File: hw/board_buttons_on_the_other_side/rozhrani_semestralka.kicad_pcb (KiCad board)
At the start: 2 copper layers, 152 x 47 mm, 63 parts, among them P1 DISPLAY_CONN, P2 DISPLAY_VCC_CON, P3 USB_B, U1 MCP2210, U2 MIC5504-3.3, U3 Joystick, U4 LM239, U5 CD4532, U6 NPIC6C596, U7 NE555, U8 PB6149L, U9 PB6149L

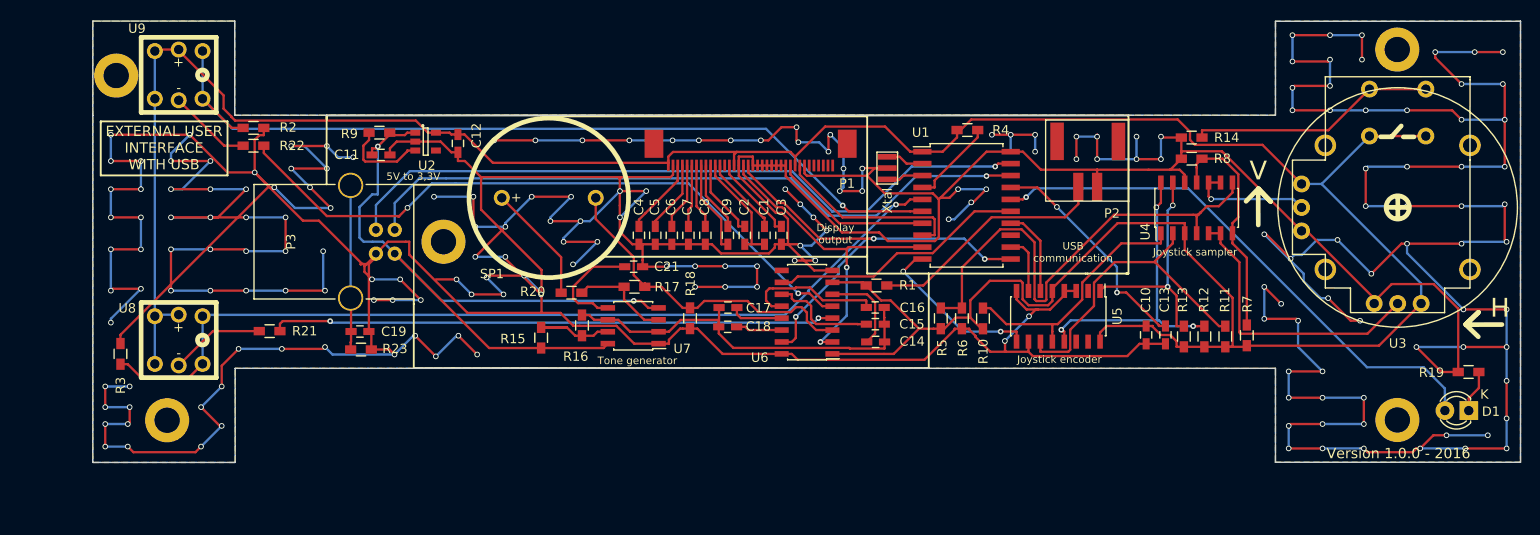
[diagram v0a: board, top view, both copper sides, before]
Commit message: first revision of caseing
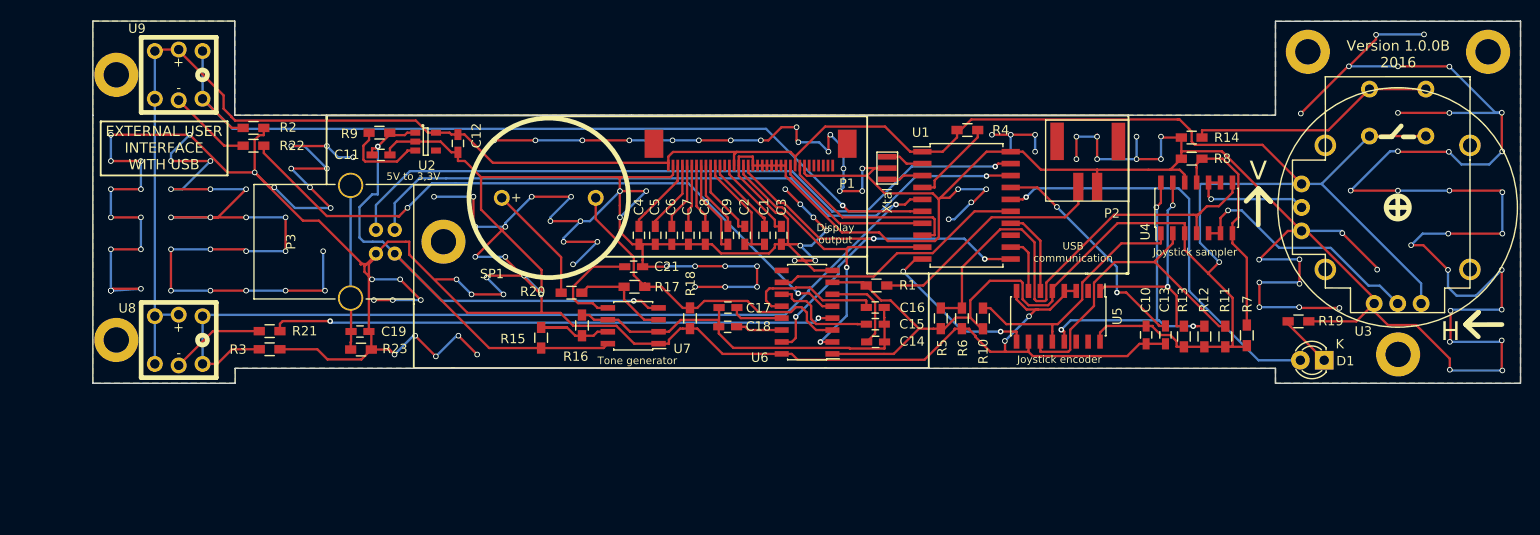
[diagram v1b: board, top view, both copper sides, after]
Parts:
- added REF**: MountingHole_2.7mm_M2.5_DIN965_Pad, Mounting_Holes:MountingHole_2.7mm_M2.5_DIN965_Pad, F.Cu at (213.7, 118.2)
- moved REF** 40.3 mm to (204.0, 86.0)
- moved R19 18.9 mm to (203.0, 114.7), turned to 180 degrees
- moved D1 16.3 mm to (205.8, 118.8)
- moved R3 15.9 mm to (93.5, 117.6), turned to 0 degrees
- moved REF** 10.1 mm to (77.2, 116.7)
- moved REF** 9.67 mm to (223.2, 86.0)
- moved REF** 0.08 mm to (77.2, 88.4)
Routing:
- net GND: track 1130.6 -> 966.4 mm, vias 195 -> 153
- net /SIGNAL_LED: track 57.9 -> 44.7 mm
- net Net-(U3-Pad9): track 30.9 -> 26.2 mm, vias 0 -> 1
- net /BUT1: track 96.8 -> 93.6 mm
- net Net-(D1-Pad1): track 4.56 -> 6.30 mm
- net +3V3: track 324.2 -> 325.5 mm, vias 0 -> 1
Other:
- board size 152 x 47 mm -> 152 x 38.6 mm
- board text added: "Version 1.0.0B 2016"
- board text removed: "Version 1.0.0 - 2016"

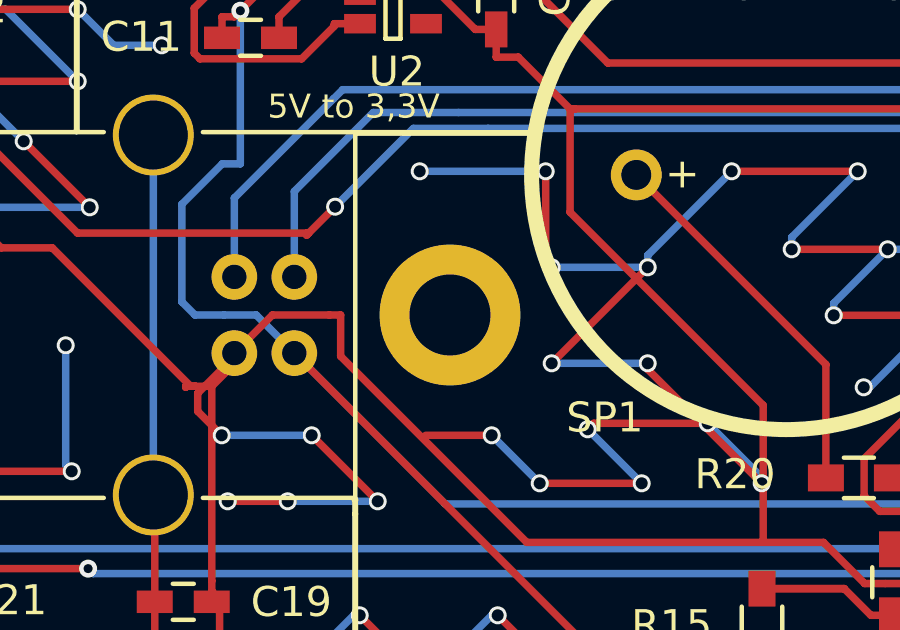
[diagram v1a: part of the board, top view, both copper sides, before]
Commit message: Just remove one mounting hole
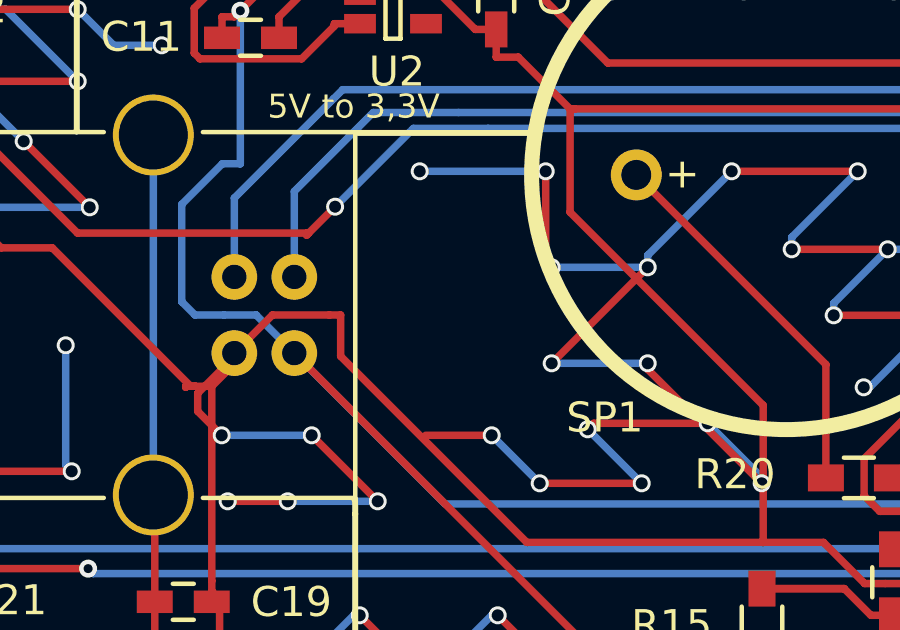
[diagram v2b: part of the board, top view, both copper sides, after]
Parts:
- removed the REF** at (112.0, 106.2)
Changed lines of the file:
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@@
     (tracks 1166)
     (zones 0)
-    (modules 64)
+    (modules 63)
     (nets 73)
   )
@@
   (module Mounting_Holes:MountingHole_2.7mm_M2.5_DIN965_Pad (layer F.Cu)
     (at 77.18 88.42)
-    (descr "Mounting Hole 2.7mm, M2.5, DIN965")
-    (tags "mounting hole 2.7mm m2.5 din965")
-    (fp_text reference REF** (at 0 -3.35) (layer Dwgs.User)
-      (effects (font (size 1 1) (thickness 0.15)))
-    )
-    (fp_text value MountingHole_2.7mm_M2.5_DIN965_Pad (at 0 3.35) (layer F.Fab)
-      (effects (font (size 1 1) (thickness 0.15)))
-    )
-    (fp_circle (center 0 0) (end 2.35 0) (layer Cmts.User) (width 0.15))
-    (fp_circle (center 0 0) (end 2.6 0) (layer F.CrtYd) (width 0.05))
-    (pad 1 thru_hole circle (at 0 0) (size 4.7 4.7) (drill 2.7) (layers *.Cu *.Mask F.SilkS))
-  )
-  (module Mounting_Holes:MountingHole_2.7mm_M2.5_DIN965_Pad (layer F.Cu)
-    (at 112.01 106.19)
     (descr "Mounting Hole 2.7mm, M2.5, DIN965")
     (tags "mounting hole 2.7mm m2.5 din965")
@@
   (segment (start 155.1344 102.955) (end 161.6997 102.955) (width 0.25) (layer F.Cu) (net 52))
   (segment (start 154.5131 102.3337) (end 155.1344 102.955) (width 0.25) (layer F.Cu) (net 52))
-  (segment (start 201.94 114.67) (end 201.94 114.97) (width 0.25) (layer F.Cu) (net 53) (status C00000))
-  (segment (start 201.94 114.97) (end 205.78 118.81) (width 0.25) (layer F.Cu) (net 53) (status C00000))
+  (segment (start 201.94 114.67) (end 201.94 114.97) (width 0.25) (layer F.Cu) (net 53))
+  (segment (start 201.94 114.97) (end 205.78 118.81) (width 0.25) (layer F.Cu) (net 53))
   (segment (start 205.38 118.41) (end 205.78 118.81) (width 0.25) (layer F.Cu) (net 53))
   (segment (start 191.39995 107.3) (end 191.39995 101.62995) (width 0.25) (layer B.Cu) (net 54))
@@
   (segment (start 124.54 107.84) (end 124.54 111.62) (width 0.25) (layer F.Cu) (net 67))
   (segment (start 118.22 101.52) (end 124.54 107.84) (width 0.25) (layer F.Cu) (net 67))
-  (segment (start 203.37 105.04) (end 207.67 105.04) (width 0.25) (layer B.Cu) (net 68) (status 400000))
+  (segment (start 203.37 105.04) (end 207.67 105.04) (width 0.25) (layer B.Cu) (net 68))
   (via (at 211.42 109.16) (size 0.6) (drill 0.4) (layers F.Cu B.Cu) (net 68))
   (segment (start 211.42 108.99) (end 211.42 109.16) (width 0.25) (layer F.Cu) (net 68))
@@
   (segment (start 224.69 96.54) (end 224.69 92.45) (width 0.25) (layer F.Cu) (net 68))
   (segment (start 224.69 96.54) (end 224.73 96.58) (width 0.25) (layer F.Cu) (net 68))
-  (segment (start 211.1 112.77) (end 211.1 113.6) (width 0.25) (layer F.Cu) (net 68) (status C00000))
-  (segment (start 211.1 113.6) (end 212.56 115.06) (width 0.25) (layer F.Cu) (net 68) (status 400000))
+  (segment (start 211.1 112.77) (end 211.1 113.6) (width 0.25) (layer F.Cu) (net 68))
+  (segment (start 211.1 113.6) (end 212.56 115.06) (width 0.25) (layer F.Cu) (net 68))
   (segment (start 223.35 97.96) (end 224.73 96.58) (width 0.25) (layer B.Cu) (net 68))
   (segment (start 224.73 96.58) (end 224.75 96.56) (width 0.25) (layer B.Cu) (net 68))
@@
   (segment (start 215.57 115.06) (end 219.15 118.64) (width 0.25) (layer F.Cu) (net 68))
   (segment (start 212.56 115.06) (end 215.57 115.06) (width 0.25) (layer F.Cu) (net 68))
-  (segment (start 203.37 105.04) (end 201.91 105.04) (width 0.25) (layer F.Cu) (net 68) (status 400000))
+  (segment (start 203.37 105.04) (end 201.91 105.04) (width 0.25) (layer F.Cu) (net 68))
   (via (at 207.4 113.24) (size 0.6) (drill 0.4) (layers F.Cu B.Cu) (net 68))
   (segment (start 203.2 113.24) (end 207.4 113.24) (width 0.25) (layer F.Cu) (net 68))
@@
   (via (at 198.85 108.1) (size 0.6) (drill 0.4) (layers F.Cu B.Cu) (net 68))
   (segment (start 201.91 105.04) (end 198.85 108.1) (width 0.25) (layer F.Cu) (net 68))
-  (segment (start 204.14 114.67) (end 209.2 114.67) (width 0.25) (layer F.Cu) (net 68) (status 400000))
-  (segment (start 209.2 114.67) (end 211.1 112.77) (width 0.25) (layer F.Cu) (net 68) (status 800000))
+  (segment (start 204.14 114.67) (end 209.2 114.67) (width 0.25) (layer F.Cu) (net 68))
+  (segment (start 209.2 114.67) (end 211.1 112.77) (width 0.25) (layer F.Cu) (net 68))
   (segment (start 94.6 117.64) (end 98.58 117.64) (width 0.25) (layer F.Cu) (net 68))
   (segment (start 103.28 118.72) (end 104.33 117.67) (width 0.25) (layer F.Cu) (net 68))

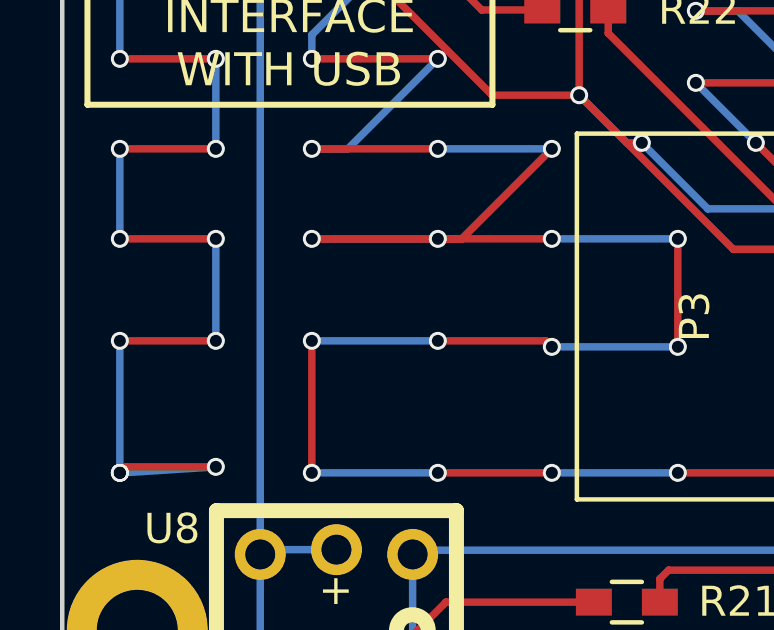
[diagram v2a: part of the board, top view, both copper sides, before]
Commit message: Added company logo + dimensions - board 1.0.0B
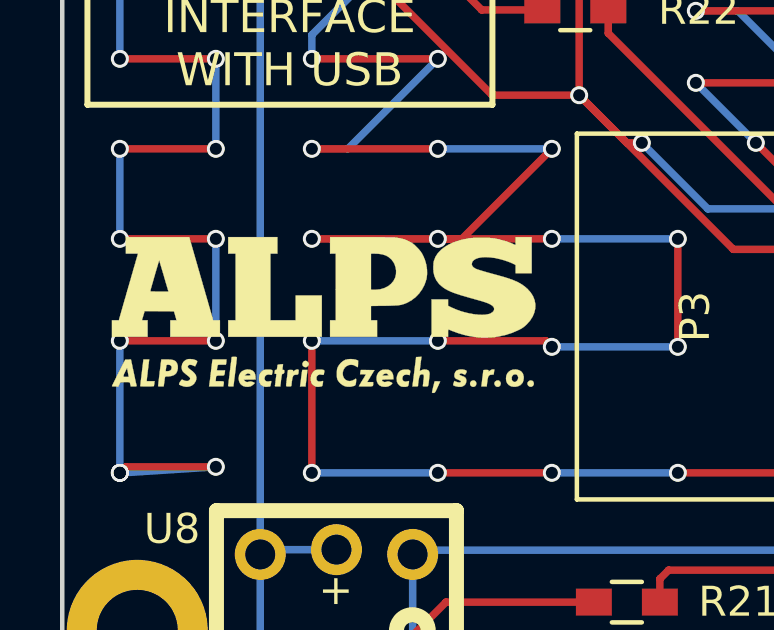
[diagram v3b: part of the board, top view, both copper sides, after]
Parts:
- added G***: LOGO, pcb:LOGO, F.Cu at (83.4, 106.1)
